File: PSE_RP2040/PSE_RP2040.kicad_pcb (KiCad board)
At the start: 2 copper layers, 85 x 56 mm, 129 parts, among them IC1 LAN8742A-CZ, IC2 SAM-M8Q-0, J1 USB_B, J2 USB_B_Mini, J3 8P8C_LED, J4 Conn_01x03, J5 Screw_Terminal_01x02, J6 Conn_01x04_Female, Q2 IRLML6402, SW1 SW_Push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

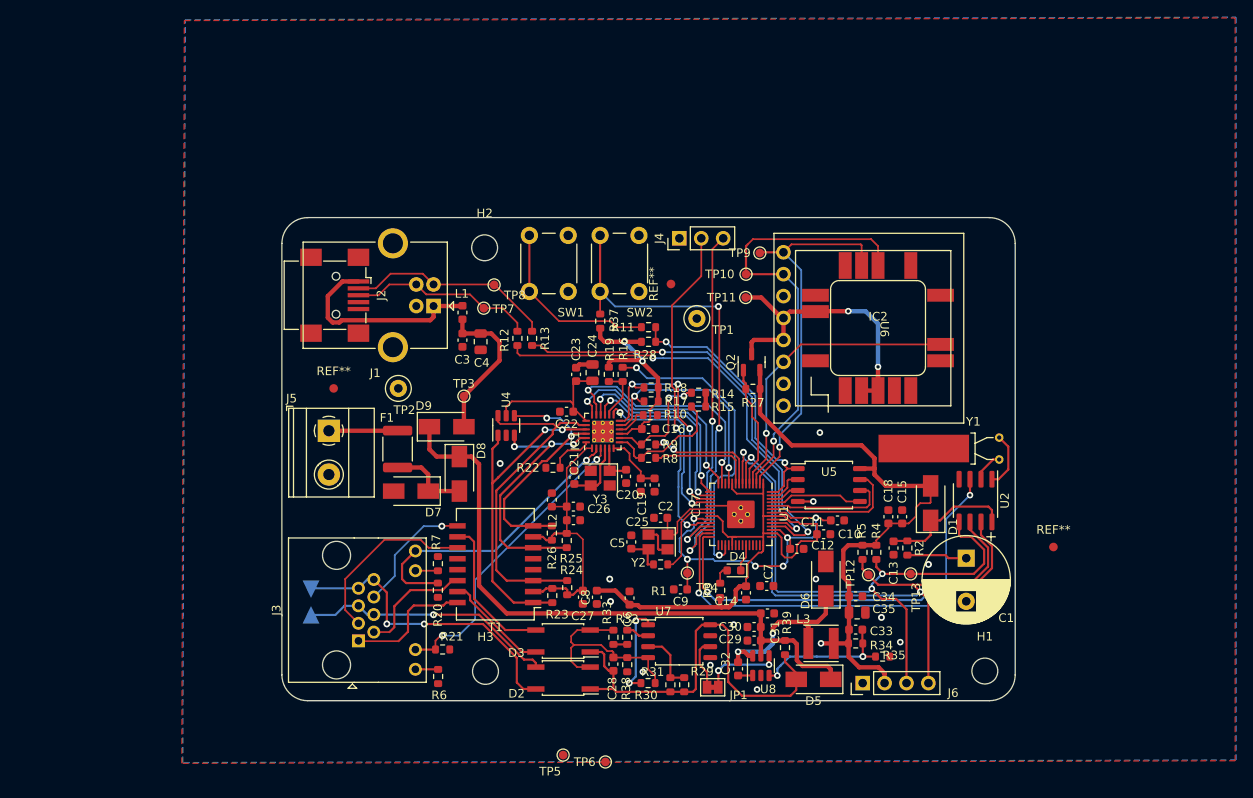
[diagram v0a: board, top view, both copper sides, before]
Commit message: sbroglio pcb, aggiunte vias
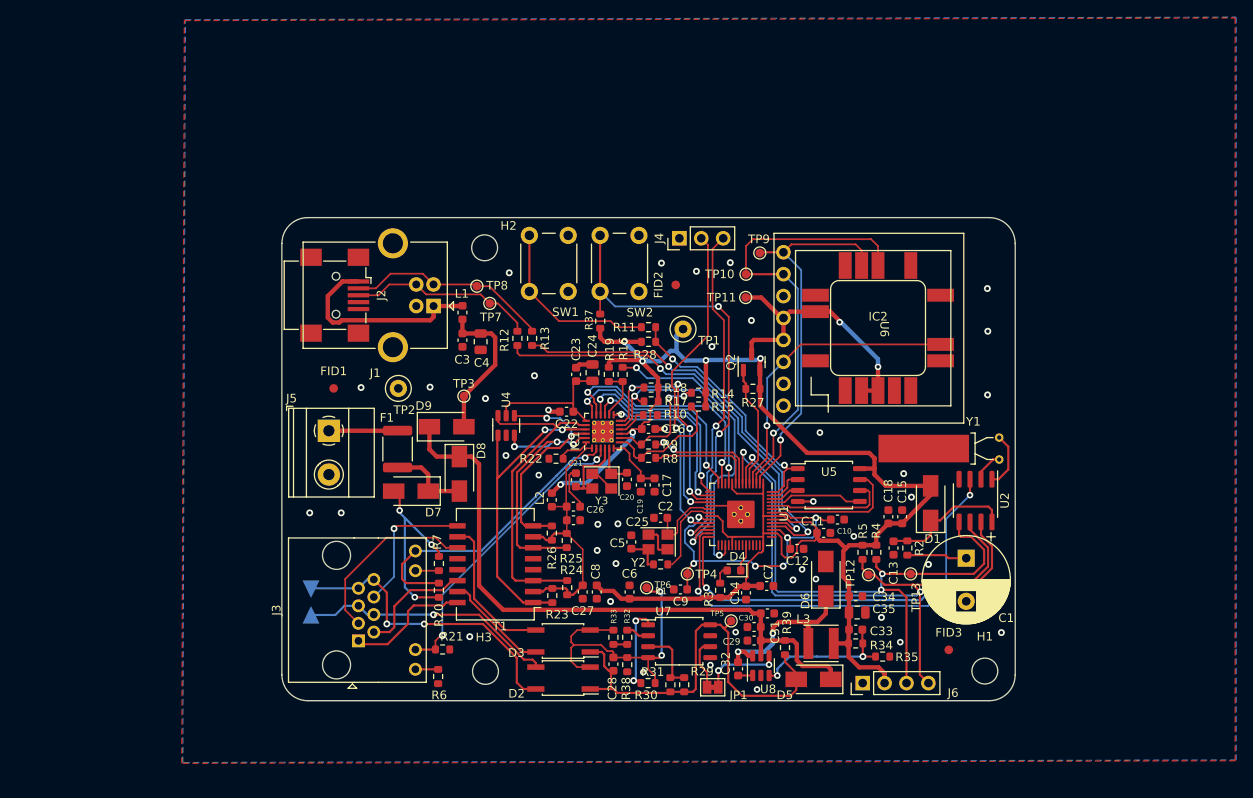
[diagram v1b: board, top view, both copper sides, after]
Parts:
- moved TP5 24.9 mm to (152.1, 148.8)
- moved TP6 20.8 mm to (142.3, 144.9)
- moved FID3 17.0 mm to (177.3, 152.1)
- moved TP1 2.02 mm to (146.5, 114.9)
- moved TP8 2.01 mm to (122.6, 110.0)
- moved R22 1.11 mm to (131.8, 129.9)
- moved TP7 0.89 mm to (124.1, 112.0)
- moved C6 0.70 mm to (140.3, 145.4)
- moved C8 0.61 mm to (136.5, 145.4)
- moved C27 0.60 mm to (134.9, 145.4)
- moved FID2 0.56 mm to (145.7, 109.8)
- moved Y3 0.39 mm to (137.1, 132.6)
- moved C20 0.36 mm to (140.0, 132.3)
- moved C21 0.35 mm to (134.1, 132.4)
- moved C10 0.15 mm to (162.8, 138.6)
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- renumbered REF** to FID1, REF** to FID2, REF** to FID3
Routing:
- net +3V3: track 164.5 -> 200.5 mm, vias 3 -> 6
- net GND: track 11.8 -> 44.4 mm, vias 13 -> 44
- net poe-: track 24.1 -> 34.6 mm, vias 0 -> 2
- net /VCC_GPS: track 34.6 -> 32.3 mm
- net Net-(IC1-Pad20): track 39.7 -> 37.5 mm
- net Net-(R13-Pad2): track 51.0 -> 49.0 mm
- net /QSPI_SS: track 31.3 -> 29.2 mm
- net Net-(IC1-Pad22): track 28.8 -> 26.8 mm
- net Net-(R12-Pad2): track 50.4 -> 48.4 mm
- net RX_N: track 14.5 -> 16.4 mm
- net Net-(IC1-Pad21): track 38.7 -> 37.0 mm
- net poe+: track 49.5 -> 51.0 mm
- net /MCU_nRST: track 57.2 -> 55.7 mm
- net Net-(C21-Pad1): track 7.41 -> 8.81 mm
- net Net-(IC1-Pad24): track 5.04 -> 3.84 mm
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
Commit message: scritte top, bottom su rame, serigrafia TP
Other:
- board text added: "BOTTOM"
- board text added: "ERRORI: 12 AVVISI: 6 TESTPOINT TP1 3V3 TP2 GND TP3 5V TP4 1V1 TP5 POE+ TP6 POE- TP7 USB_DP TP8 USB_DN TP9 UART_TX-GPS_RX TP10 UART_RX-GPS_TX TP11 VCC_GPS TP12 GPIO3_I2C_SCL TP13 GPIO2_I2C_SDA"
- board text added: "TOP"
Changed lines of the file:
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@@
     (property "Sheetname" "")
     (attr exclude_from_pos_files)
-    (fp_text reference "TP6" (at 1.875 -0.325002) (layer "F.SilkS")
+    (fp_text reference "TP6" (at 1.775 -0.7) (layer "F.SilkS")
       (effects (font (size 0.762 0.762) (thickness 0.1143)))
     )
@@
     (property "Sheetname" "")
     (attr smd)
-    (fp_text reference "R7" (at -2.5 0.2 90) (layer "F.SilkS")
+    (fp_text reference "R7" (at -2.475 -0.225 90) (layer "F.SilkS")
       (effects (font (size 1 1) (thickness 0.15)))
     )
@@
     (property "Sheetname" "")
     (attr exclude_from_pos_files)
-    (fp_text reference "TP5" (at -1.625 -0.85) (layer "F.SilkS")
-      (effects (font (size 0.635 0.635) (thickness 0.15)))
+    (fp_text reference "TP5" (at -1.55 -0.85) (layer "F.SilkS")
+      (effects (font (size 0.635 0.635) (thickness 0.1143)))
     )
     (fp_text value "POE+" (at 0 1.55) (layer "F.Fab")
@@
     (property "Sheetname" "")
     (attr smd)
-    (fp_text reference "D4" (at -0.425 1.6) (layer "F.SilkS")
+    (fp_text reference "D4" (at -0.05 1.35) (layer "F.SilkS")
       (effects (font (size 1 1) (thickness 0.15)))
     )
@@
     (property "Sheetname" "")
     (attr exclude_from_pos_files)
-    (fp_text reference "TP4" (at 2.2 0.05) (layer "F.SilkS")
+    (fp_text reference "TP4" (at 2.15 0.05) (layer "F.SilkS")
       (effects (font (size 1 1) (thickness 0.15)))
     )
@@
     (property "Sheetname" "")
     (attr through_hole)
-    (fp_text reference "J3" (at 3.56 -9.5 90) (layer "F.SilkS")
+    (fp_text reference "J3" (at 12.71 0.075 180) (layer "F.SilkS")
       (effects (font (size 1 1) (thickness 0.15)))
     )
@@
     (property "Sheetname" "")
     (attr smd)
-    (fp_text reference "U1" (at -0.1 -5 90) (layer "F.SilkS")
+    (fp_text reference "U1" (at -4.95 -0.4 180) (layer "F.SilkS")
       (effects (font (size 1 1) (thickness 0.15)))
     )
@@
     (property "Sheetname" "")
     (attr smd)
-    (fp_text reference "R1" (at -0.050004 -3.099989) (layer "F.SilkS")
+    (fp_text reference "R1" (at -2.15 0.25) (layer "F.SilkS")
       (effects (font (size 0.762 0.762) (thickness 0.1143)))
     )
@@
     (property "Sheetname" "")
     (attr smd)
-    (fp_text reference "J2" (at 0 -5.25 90) (layer "F.SilkS")
+    (fp_text reference "J2" (at -6.85 0.575 180) (layer "F.SilkS")
       (effects (font (size 1 1) (thickness 0.15)))
     )
@@
   (gr_line (start 0 0) (end 85 0) (layer "User.6") (width 0.15))
   (gr_circle (center 61.5 3.5) (end 64.5 3.5) (layer "User.6") (width 0.15) (fill none))
+  (gr_text "TOP" (at 182.7 114.575 90) (layer "F.Cu")
+    (effects (font (size 1 1) (thickness 0.15)))
+  )
+  (gr_text "BOTTOM" (at 182.625009 114.724993 270) (layer "B.Cu")
+    (effects (font (size 1 1) (thickness 0.15)) (justify mirror))
+  )
+  (gr_text "ERRORI: 12\nAVVISI: 6\n\nTESTPOINT\nTP1 3V3\nTP2 GND\nTP3 5V\nTP4 1V1\nTP5 POE+\nTP6 POE-\nTP7 USB_DP\nTP8 USB_DN\nTP9 UART_TX-GPS_RX\nTP10 UART_RX-GPS_TX\nTP11 VCC_GPS\nTP12 GPIO3_I2C_SCL\nTP13 GPIO2_I2C_SDA" (at 69.325 126.275) (layer "F.SilkS")
+    (effects (font (size 1 1) (thickness 0.15)) (justify left))
+  )
   (gr_text "footprint Rpi4\n" (at 37.5 31.25) (layer "User.6")
     (effects (font (size 1 1) (thickness 0.15)))
@@
   (via (at 169.5 148.35) (size 0.8) (drill 0.4) (layers "F.Cu" "B.Cu") (free) (net 16))
   (via (at 151.975 107.225) (size 0.8) (drill 0.4) (layers "F.Cu" "B.Cu") (free) (net 16))
-  (via (at 181.8 122.55) (size 0.8) (drill 0.4) (layers "F.Cu" "B.Cu") (free) (net 16))
+  (via (at 182.925 124.2) (size 0.8) (drill 0.4) (layers "F.Cu" "B.Cu") (free) (net 16))
   (via (at 160.3 142.775) (size 0.762) (drill 0.381) (layers "F.Cu" "B.Cu") (net 16))
   (via (at 117.175 121.65) (size 0.8) (drill 0.4) (layers "F.Cu" "B.Cu") (free) (net 16))
@@
   (via (at 172.075 131.675) (size 0.8) (drill 0.4) (layers "F.Cu" "B.Cu") (free) (net 16))
   (via (at 136.625 137.55) (size 0.8) (drill 0.4) (layers "F.Cu" "B.Cu") (free) (net 16))
-  (via (at 181.825 115.175) (size 0.8) (drill 0.4) (layers "F.Cu" "B.Cu") (free) (net 16))
+  (via (at 180.4 120.075) (size 0.8) (drill 0.4) (layers "F.Cu" "B.Cu") (free) (net 16))
   (via (at 138.1 146.5) (size 0.8) (drill 0.4) (layers "F.Cu" "B.Cu") (free) (net 16))
   (via (at 148.05 108.225) (size 0.8) (drill 0.4) (layers "F.Cu" "B.Cu") (free) (net 16))

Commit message: Leggi descrizione per verifica
-tolte aree rame sotto pin non usati.
-spostate le serigrafie
-portato a 11 gli errori, da verificare se
VDD1A e VDD2A di IC1 devono essere connessi? ->Errori ridotti a 11
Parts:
- moved TP11 2.78 mm to (155.1, 113.7)
- moved TP10 1.30 mm to (155.1, 108.5)
- moved TP9 0.32 mm to (155.1, 106.0)
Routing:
- net Net-(C22-Pad1): track 48.2 -> 66.0 mm, vias 0 -> 2
- net /VCC_GPS: track 32.3 -> 29.9 mm
- net /UART_RX-GPS_TX: track 52.9 -> 52.1 mm
- net GND: vias 44 -> 49
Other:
- board text added: "VDD1A e VDD2A di IC1 devono essere connessi? ->Errori ridotti a 11"

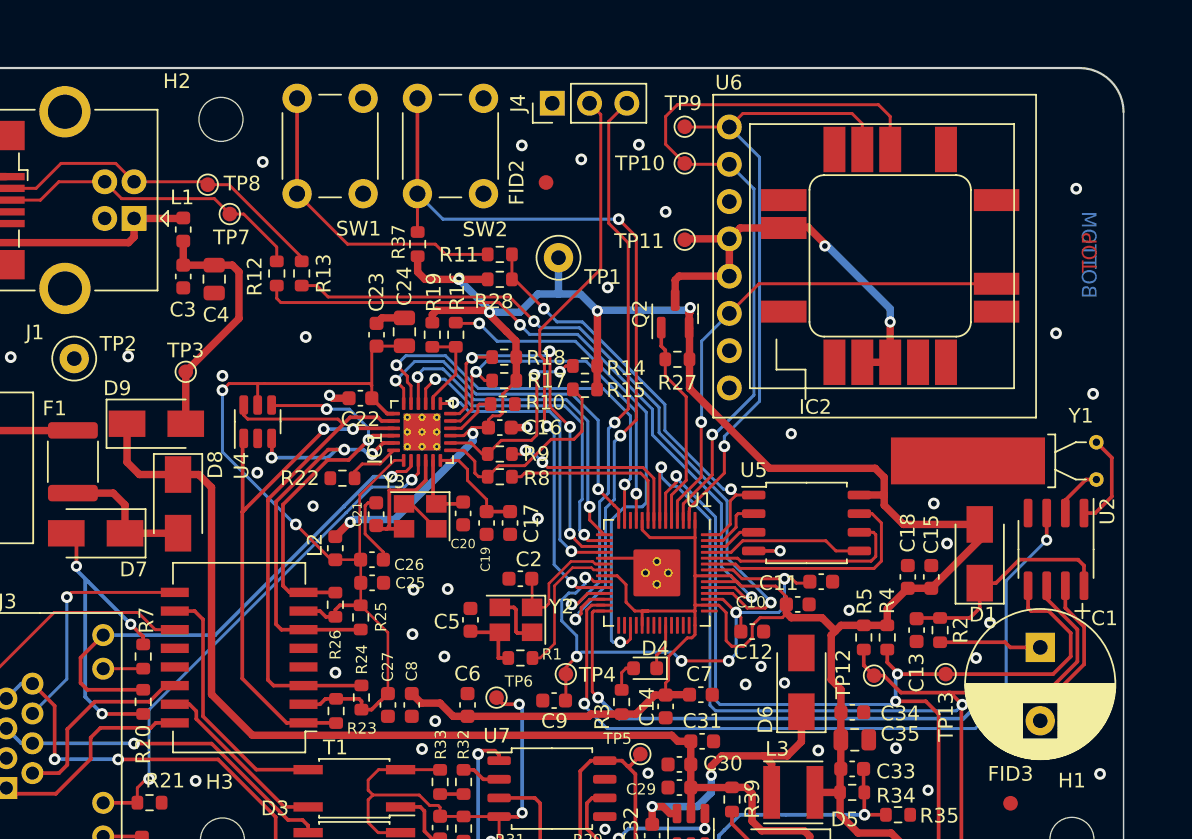
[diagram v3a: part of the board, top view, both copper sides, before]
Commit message: footprint micro con piazzole paste, gerber
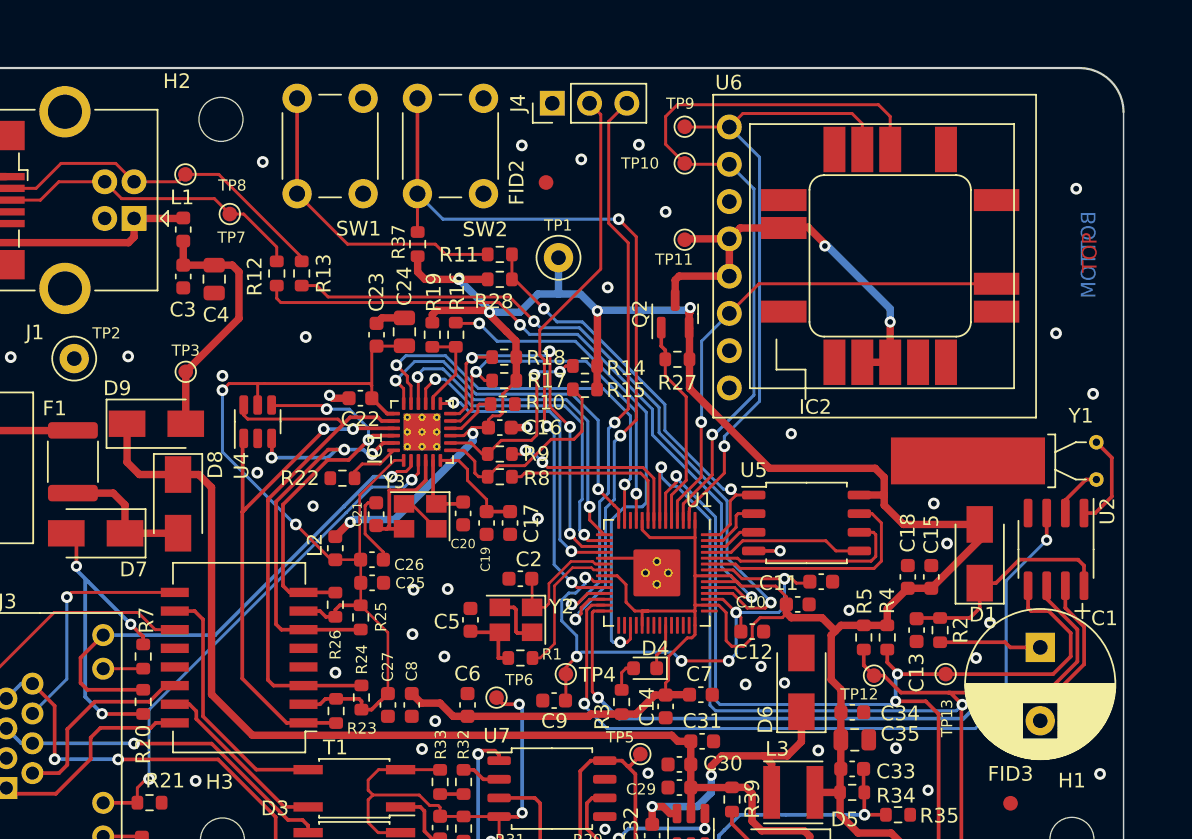
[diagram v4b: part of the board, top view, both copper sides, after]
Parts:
- moved TP8 1.68 mm to (121.1, 109.2)
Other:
- board text added: ">Errori ridotti a 11"
- board text removed: "VDD1A e VDD2A di IC1 devono essere connessi? ->Errori ridotti a 11"

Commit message: ottimizzazioni
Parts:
- D1: value D_Schottky -> BAT54C; footprint Diode_SMD:D_SMA -> Package_TO_SOT_SMD:SOT-23
- moved C18 10.3 mm to (167.1, 126.9), turned to 0 degrees
- moved C15 9.50 mm to (167.1, 128.5), turned to 0 degrees
- moved R1 4.46 mm to (146.2, 138.4), turned to -90 degrees
- moved C5 3.79 mm to (143.6, 141.8), turned to 180 degrees
- moved C2 3.48 mm to (140.8, 138.4), turned to -90 degrees
- moved C20 1.05 mm to (141.0, 132.6)
- moved C17 1.03 mm to (144.2, 133.0)
- moved C19 1.03 mm to (142.6, 133.0)
- moved C21 1.03 mm to (135.1, 132.4)
- moved Y3 1.03 mm to (138.1, 132.6)
- moved Y2 0.92 mm to (143.6, 138.7), turned to -90 degrees
- moved U5 0.83 mm to (163.8, 132.3)
- moved D1 0.70 mm to (174.5, 135.1), turned to -90 degrees
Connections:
- C13 pad 1: Net-(C13-Pad1) -> Net-(U2-Pad8)
- D1 pad 1: Net-(C13-Pad1) -> +3V3
- R2 pad 2: Net-(C13-Pad1) -> Net-(U2-Pad8)
- U2 pad 8: Net-(C13-Pad1) -> Net-(U2-Pad8)
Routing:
- net Net-(U2-Pad8): track 0.00 -> 16.9 mm
- net Net-(C13-Pad1): track 15.6 -> 0.00 mm
- net GND: track 44.4 -> 33.6 mm, vias 49 -> 51
- net Net-(R1-Pad1): track 9.92 -> 4.25 mm
- net +3V3: track 200.2 -> 204.4 mm, vias 6 -> 8
- net /PPS: track 34.6 -> 37.6 mm, vias 1 -> 3
- net Net-(C21-Pad1): track 8.81 -> 7.46 mm
- net /RTC_CLKOUT: track 48.0 -> 48.9 mm
- net Net-(C2-Pad1): track 9.05 -> 9.86 mm
- net /QSPI_SCLK: track 14.2 -> 15.0 mm
- net Net-(C20-Pad1): track 4.93 -> 5.69 mm
- net /VCC_GPS: track 29.9 -> 30.7 mm, vias 2 -> 0
- net /QSPI_SD1: track 4.25 -> 4.95 mm
- net /QSPI_SD2: track 3.42 -> 4.13 mm
- net /QSPI_SS: track 29.2 -> 29.9 mm
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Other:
- board text added: "3V3"
- board text added: "GND"

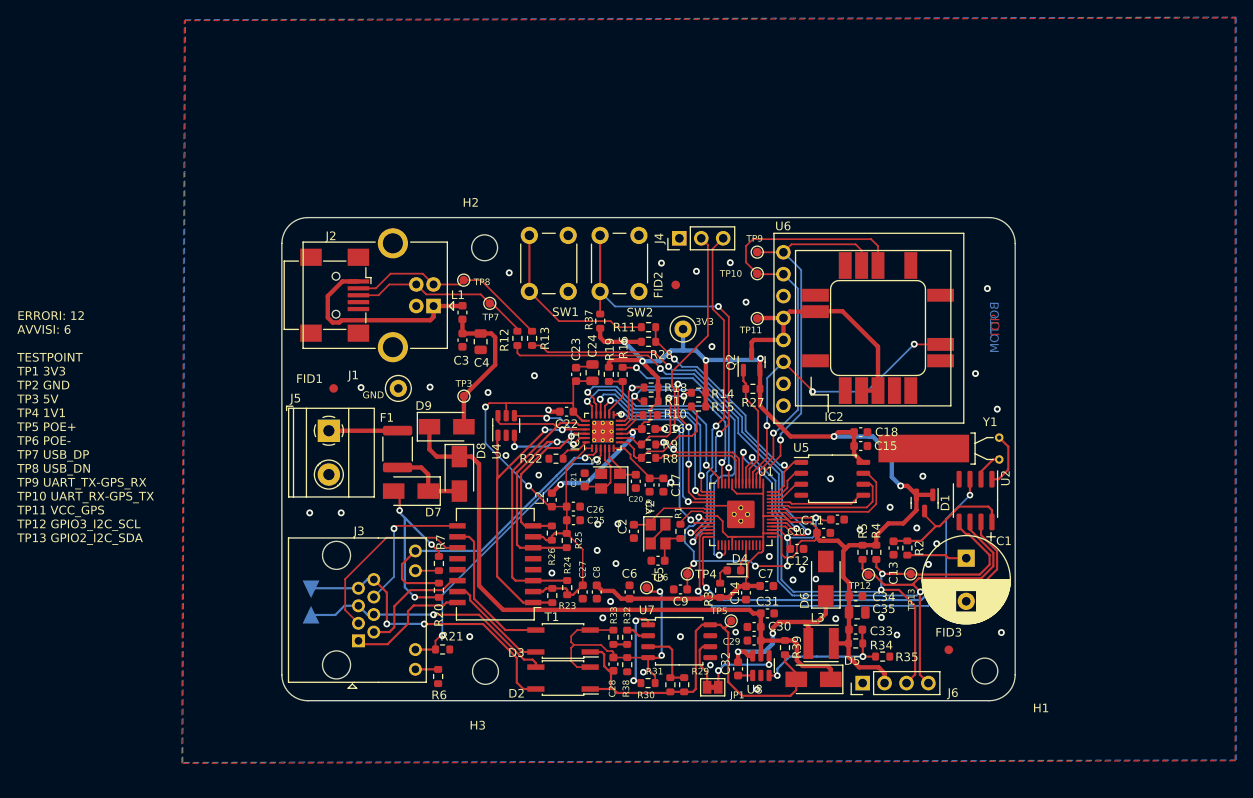
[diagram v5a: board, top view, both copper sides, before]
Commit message: impronta pam7 (pad saldatura)
TODO: rigenerare gerber
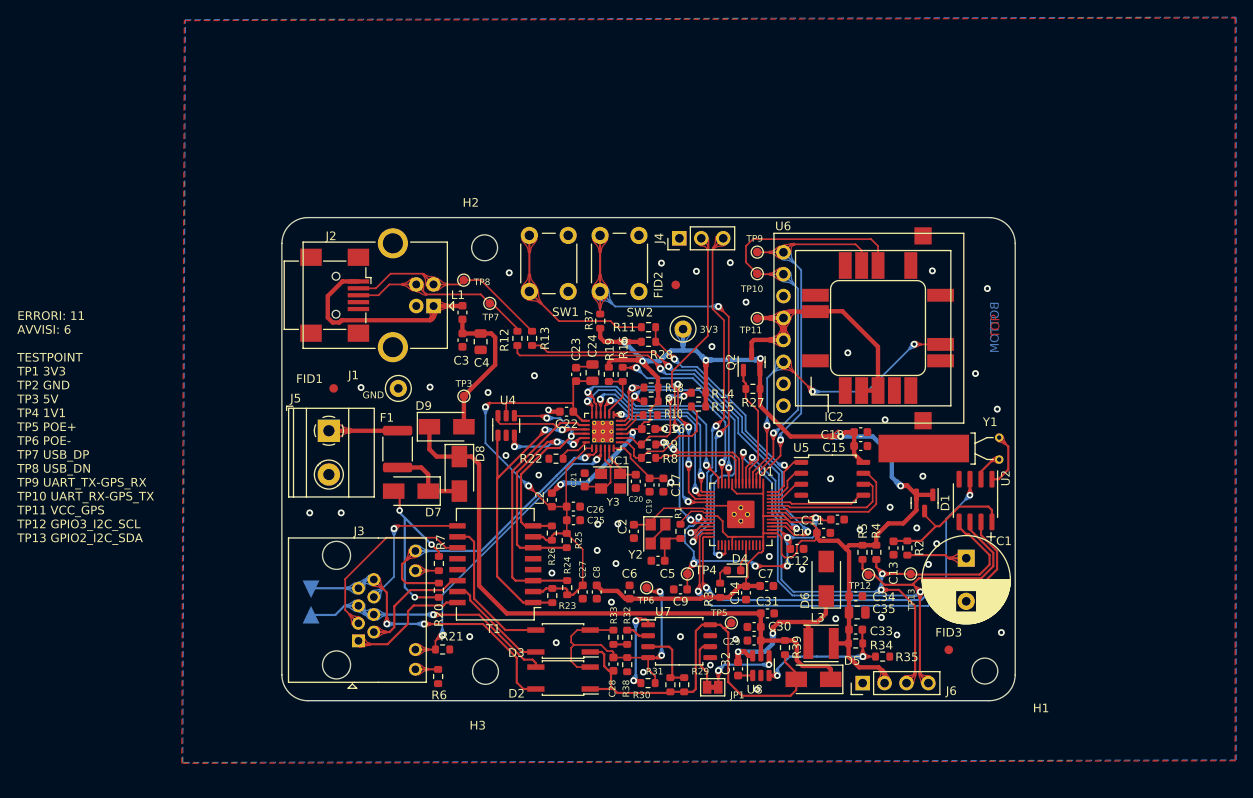
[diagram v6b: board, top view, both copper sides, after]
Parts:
- moved TP5 0.23 mm to (152.1, 149.0)
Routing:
- net +3V3: track 204.4 -> 203.4 mm
- net GND: vias 51 -> 52
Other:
- board text added: "ERRORI: 11 AVVISI: 6 TESTPOINT TP1 3V3 TP2 GND TP3 5V TP4 1V1 TP5 POE+ TP6 POE- TP7 USB_DP TP8 USB_DN TP9 UART_TX-GPS_RX TP10 UART_RX-GPS_TX TP11 VCC_GPS TP12 GPIO3_I2C_SCL TP13 GPIO2_I2C_SDA"
- board text added: "PPE2021_LAN_NTP P.A. 209926 P.G. 209048 T.E. 209212 A.M. 209615 T.G. 209359"
- board text removed: "ERRORI: 12 AVVISI: 6 TESTPOINT TP1 3V3 TP2 GND TP3 5V TP4 1V1 TP5 POE+ TP6 POE- TP7 USB_DP TP8 USB_DN TP9 UART_TX-GPS_RX TP10 UART_RX-GPS_TX TP11 VCC_GPS TP12 GPIO3_I2C_SCL TP13 GPIO2_I2C_SDA"
